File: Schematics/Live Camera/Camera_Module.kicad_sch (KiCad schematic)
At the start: 95 parts, among them J1 Stack Male Edge Connector, J2 SWD_01x04_Pin, J4 Therm_In, J4 USB_C_Female_USB2_Small, J5 VTX, J6 RunCam6, J7 VTX_BATT_IN, J8 VTX_BATT_SWITCH, Q3 AO3400A, Q3 AO3401A, Q4 AO3400A, Q5 AO3401A, Q6 AO3401A, SW1 SW_STM_RESET, SW2 SW_STM_BOOT_MODE, U1 CP2102N-Axx-xQFN28, U1 LM66100DCKR, U1 STM32F103CBT6, U12 AMS1117-3.3, U3 W25Q128JVS, U5 LM66100DCKR, U6 LM66100DCKR, U8 ISO1042BDWVR, Y1 X322516MMB4SI

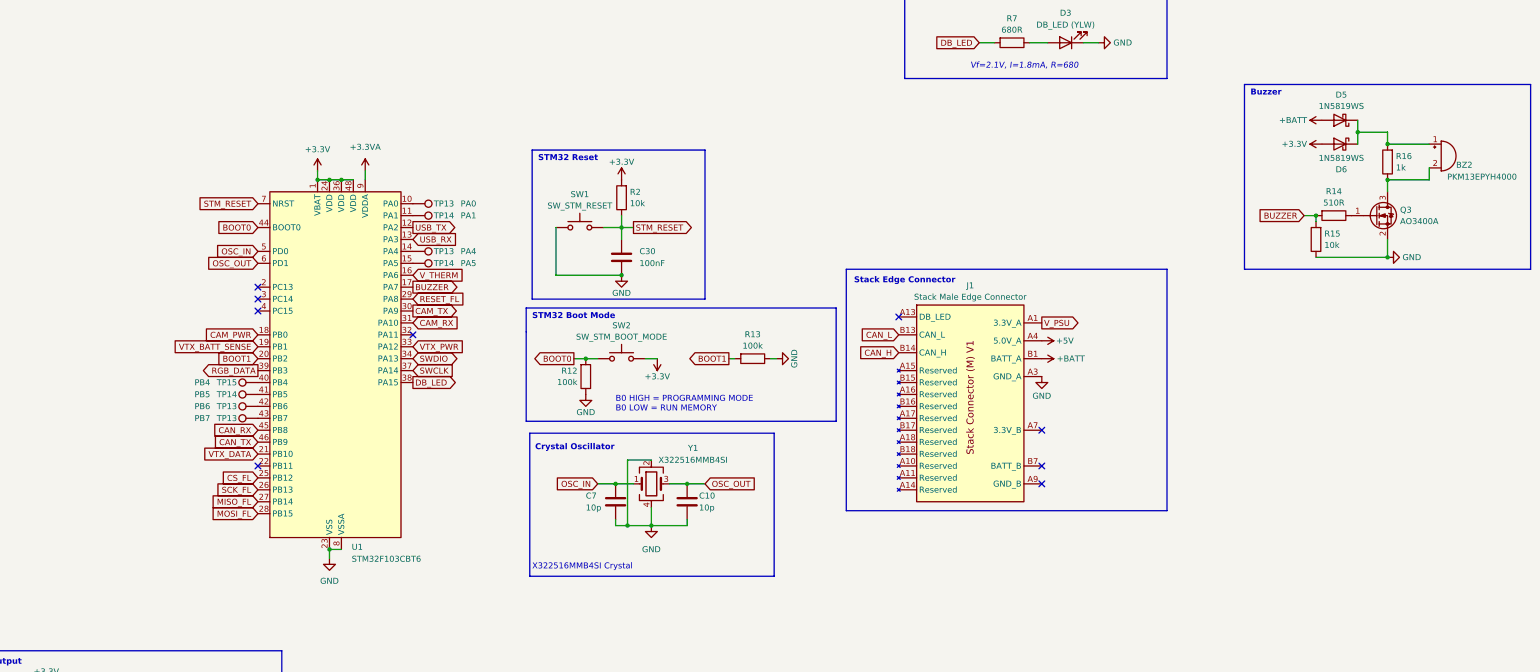
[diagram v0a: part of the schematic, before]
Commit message: Added revised buzzer circuit
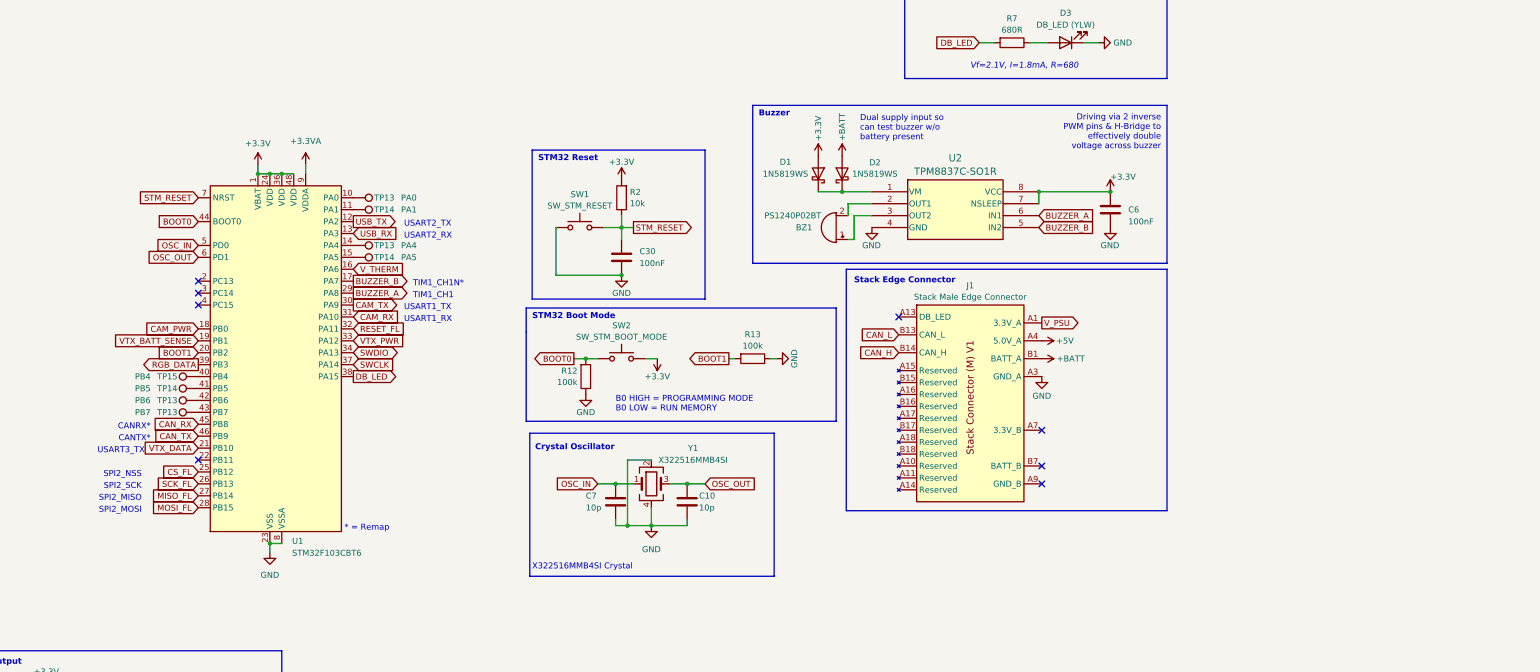
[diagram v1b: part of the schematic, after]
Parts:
- removed BZ2: PKM13EPYH4000, footprints:Buzzer_12.6x9.5RM5.0, symbol Device:Buzzer
- removed D5, D6: 1N5819WS, Diode_SMD:D_SOD-323, symbol Diode:1N5819WS
- removed Q3: AO3400A, Package_TO_SOT_SMD:SOT-23, symbol Transistor_FET:AO3400A
- removed R14: 510R, Resistor_SMD:R_0603_1608Metric, symbol Device:R
- removed R15: 10k, Resistor_SMD:R_0603_1608Metric, symbol Device:R
- removed R16: 1k, Resistor_SMD:R_0603_1608Metric, symbol Device:R
- added BZ1: PS1240P02BT, footprints:Buzzer_12.6x9.5RM5.0, symbol Device:Buzzer
- added C6: 100nF, Capacitor_SMD:C_0603_1608Metric, symbol Device:C
- added D1, D2: 1N5819WS, Diode_SMD:D_SOD-323, symbol Diode:1N5819WS
- added U2: TPM8837C-SO1R, footprints:SOP-8_TPK, symbol TPM8837C-SO1R:TPM8837C-SO1R
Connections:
- net +3.3V: now also C6.1, D1.2 (A), U2.7 (NSLEEP), U2.8 (VCC)
- net +BATT: now also D2.2 (A)
- net GND: now also C6.2, U2.4 (GND)
- net RESET_FL: now also U1.32 (PA11); no longer U1.29 (PA8)
- net BUZZER renamed BUZZER_B
- net BUZZER_B: now also U2.5 (IN2)
- new net: BZ1.1 (-), U2.3 (OUT2)
- new net: BZ1.2 (+), U2.2 (OUT1)
- new net: D1.1 (K), D2.1 (K), U2.1 (VM)
- new net BUZZER_A: U1.29 (PA8), U2.6 (IN1)
- no-connect marks 31 -> 30
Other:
- note added: "* = Remap"
- note added: "CANRX*"
- note added: "CANTX*"
- note added: "Driving via 2 inverse PWM pins & H-Bridge to effectively double voltage across buzzer"
- note added: "Dual supply input so can test buzzer w/o battery present"
- note added: "SPI2_MISO"
- note added: "SPI2_MOSI"
- note added: "SPI2_NSS"
- note added: "SPI2_SCK"
- note added: "TIM1_CH1"
- note added: "TIM1_CH1N*"
- note added: "USART1_RX"
- note added: "USART1_TX"
- note added: "USART2_RX"
- note added: "USART2_TX"
- note added: "USART3_TX"
- moved on the sheet: TP13, TP14, TP15, U1

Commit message: Tweaked part fields
Changed "LCSC" fields to "JLCPCB", and added missing JLCPCB/Digikey part numbers.

There may be some minor mismatches hiding somewhere; should do a manual review.
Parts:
- C10, C7: JLCPCB (none) -> C1634; LCSC C1634 -> (none)
- C11, C3, C31, C32: JLCPCB (none) -> C96446; LCSC C96446 -> (none)
- C12, C13, C15, C17: JLCPCB (none) -> C1525; LCSC C1525 -> (none)
- C19: JLCPCB (none) -> C57112; LCSC C57112 -> (none)
- C2, C3, C4, C6: JLCPCB (none) -> C15849; LCSC C15849 -> (none)
- C20, C21: JLCPCB (none) -> C28323; LCSC C28323 -> (none)
- C22, C23, C30, C8: JLCPCB (none) -> C14663; LCSC C14663 -> (none)
- D1: JLCPCB (none) -> C2297; LCSC C2297 -> (none)
- D3: JLCPCB (none) -> C72038; LCSC C72038 -> (none)
- FB1: JLCPCB (none) -> C1015; LCSC C1015 -> (none)
- J2: Digikey (none) -> 952-3233-ND
- J4: JLCPCB (none) -> C2936184; LCSC C2936184 -> (none)
- J4: Digikey (none) -> ED10561-ND
- J6: Digikey (none) -> ED10563-ND
- Q3, Q5, Q6: JLCPCB (none) -> C15127; LCSC C15127 -> (none)
- Q4: JLCPCB (none) -> C20917; LCSC C20917 -> (none)
- R10, R12, R13, R14, R38: JLCPCB (none) -> C25803; LCSC C25803 -> (none)
- R11, R39: JLCPCB (none) -> C23193; LCSC C23193 -> (none)
- R15: JLCPCB (none) -> C4184
- R2, R4, R6: JLCPCB (none) -> C25804; LCSC C25804 -> (none)
- R28, R29: JLCPCB (none) -> C23186; LCSC C23186 -> (none)
- R29: JLCPCB (none) -> C21190; LCSC C21190 -> (none)
- R30: JLCPCB (none) -> C31850; LCSC C31850 -> (none)
- R31: JLCPCB (none) -> C25819; LCSC C25819 -> (none)
- R5: JLCPCB (none) -> C22978; LCSC C22978 -> (none)
- R6: JLCPCB (none) -> C25804
- R7: JLCPCB (none) -> C23228; LCSC C23228 -> (none)
- R8: JLCPCB (none) -> C22843; LCSC C22843 -> (none)
- SW1, SW2: JLCPCB (none) -> C318884; LCSC C318884 -> (none)
- U1, U5, U6: JLCPCB (none) -> C2869734; LCSC C2869734 -> (none)
- U1: JLCPCB (none) -> C6568; LCSC C6568 -> (none)
- U1: JLCPCB (none) -> C8304; LCSC C8304 -> (none)
- U12: JLCPCB (none) -> C6186; LCSC C6186 -> (none)
- U3: JLCPCB (none) -> C97521; LCSC C97521 -> (none)
- U8: JLCPCB (none) -> C484409; LCSC C484409 -> (none)
- Y1: JLCPCB (none) -> C13738; LCSC C13738 -> (none)

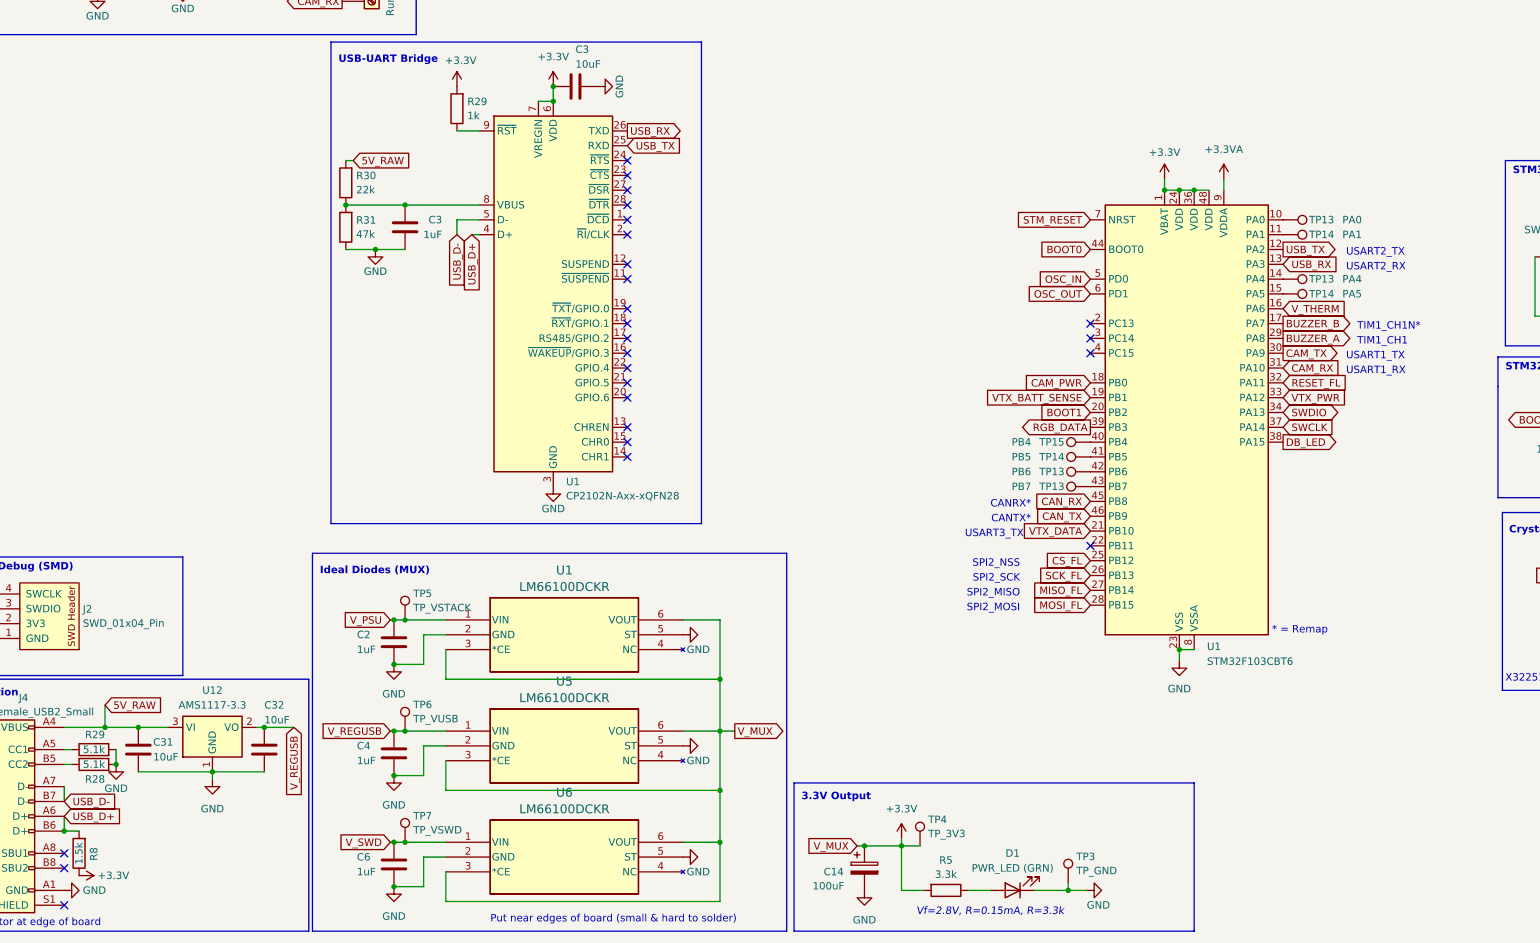
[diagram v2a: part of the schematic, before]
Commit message: Tweaks + 3D model additions
Added/tweaked some notes in the schematic, adjusted silkscreen on PCB + added "PB-FREE" label, updated SWD footprint, and added all missing 3D models to project.
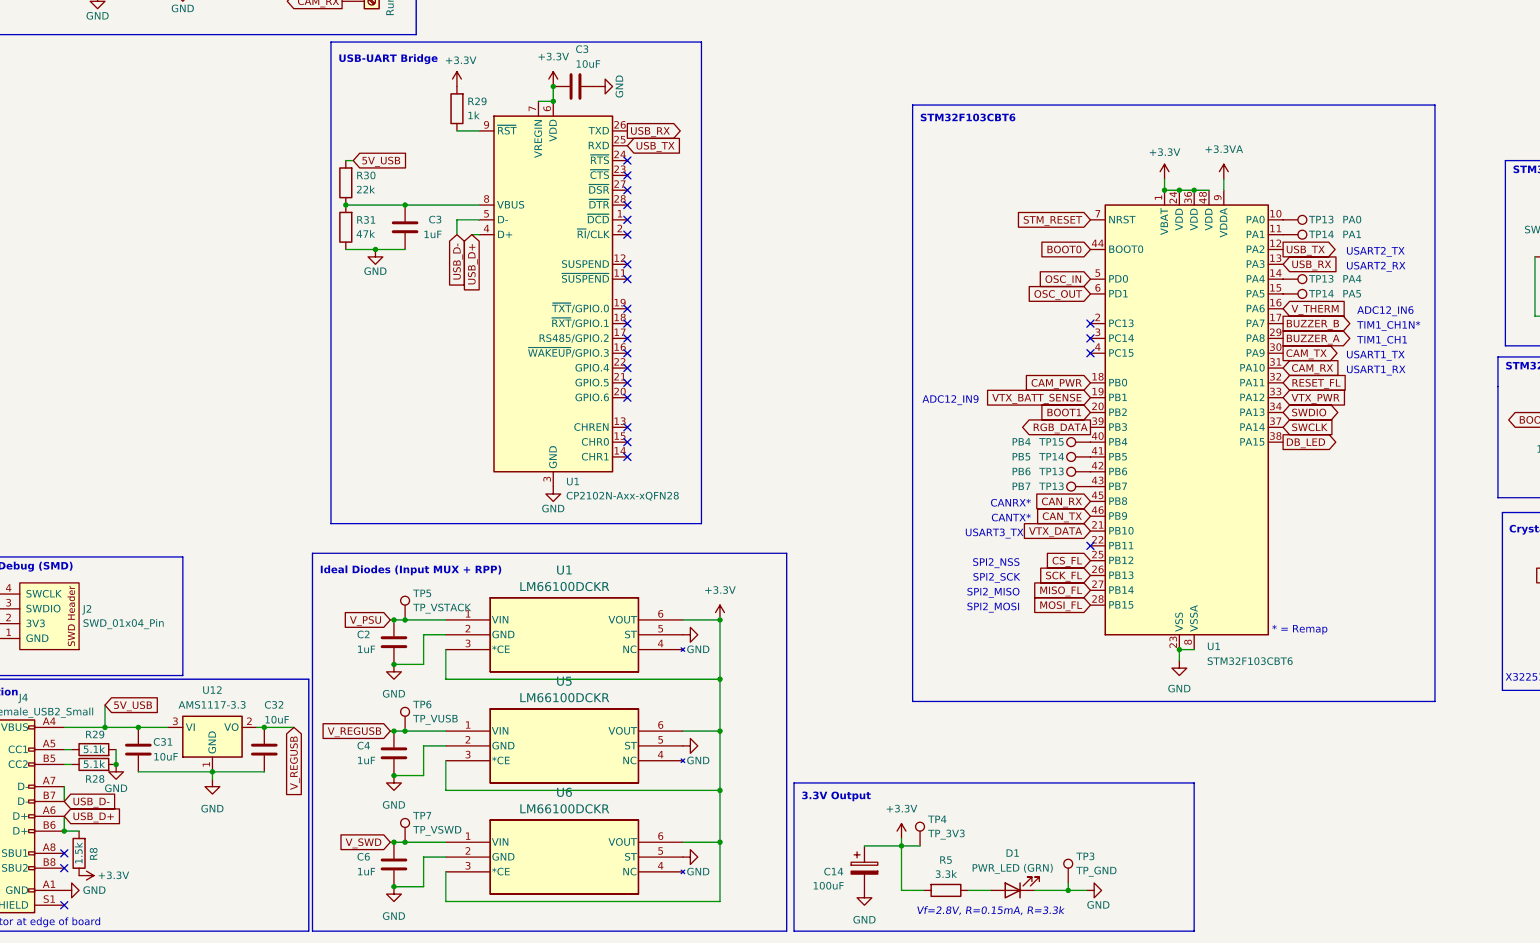
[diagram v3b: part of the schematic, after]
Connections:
- net 5V_RAW renamed 5V_USB
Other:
- note added: "ADC12_IN6"
- note added: "ADC12_IN9"
- note added: "Ideal Diodes (Input MUX + RPP)"
- note added: "STM32F103CBT6"
- note removed: "Ideal Diodes (MUX)"
- note removed: "Put near edges of board (small & hard to solder)"
- title: QRET 24-25 SRAD Camera Module (????) -> QRET 24-25 SRAD Camera Module (FizzBuzz? Ocellus?)
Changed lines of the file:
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@@
 	(paper "B")
 	(title_block
-		(title "QRET 24-25 SRAD Camera Module (????)")
-		(date "2025-02-20")
+		(title "QRET 24-25 SRAD Camera Module (FizzBuzz? Ocellus?)")
+		(date "2025-02-26")
 		(rev "V1.0")
 		(company "Queen's Rocket Engineering Team")
@@
 	)
 	(junction
+		(at 149.225 213.36)
+		(diameter 0)
+		(color 0 0 0 0)
+	)
+	(junction
 		(at 407.035 143.51)
 		(diameter 0)
@@
 	)
 	(junction
-		(at 173.99 252.095)
-		(diameter 0)
-		(color 0 0 0 0)
-	)
-	(junction
 		(at 172.72 40.005)
 		(diameter 0)
@@
 	(wire
 		(pts
-			(xy 172.72 252.095) (xy 173.99 252.095)
-		)
-		(stroke
-			(width 0)
-			(type default)
-		)
-	)
-	(wire
-		(pts
 			(xy 351.155 146.05) (xy 356.235 146.05)
 		)
@@
 	(wire
 		(pts
-			(xy 149.225 232.41) (xy 151.765 232.41)
-		)
-		(stroke
-			(width 0)
-			(type default)
-		)
-	)
-	(wire
-		(pts
 			(xy 25.4 48.895) (xy 44.45 48.895)
 		)
@@
 	)
 	(rectangle
+		(start 182.245 125.095)
+		(end 271.78 227.33)
+		(stroke
+			(width 0)
+			(type default)
+		)
+		(fill
+			(type none)
+		)
+	)
+	(rectangle
 		(start 339.725 59.69)
 		(end 361.95 97.155)
@@
 		)
 	)
-	(text "Put near edges of board (small & hard to solder)"
-		(exclude_from_sim no)
-		(at 109.855 265.43 0)
-		(effects
-			(font
-				(size 1.27 1.27)
-			)
-			(justify left bottom)
-		)
-	)
 	(text "Additional Filtering for Analogue VDD"
 		(exclude_from_sim no)
@@
 		)
 	)
+	(text "ADC12_IN9"
+		(exclude_from_sim no)
+		(at 193.675 176.53 0)
+		(effects
+			(font
+				(size 1.27 1.27)
+			)
+			(justify right bottom)
+		)
+	)
 	(text "Crystal Oscillator"
 		(exclude_from_sim no)
@@
 		)
 	)
+	(text "STM32F103CBT6"
+		(exclude_from_sim no)
+		(at 183.515 128.27 0)
+		(effects
+			(font
+				(size 1.27 1.27)
+				(thickness 0.254)
+				(bold yes)
+			)
+			(justify left bottom)
+		)
+	)
+	(text "ADC12_IN6"
+		(exclude_from_sim no)
+		(at 258.445 161.29 0)
+		(effects
+			(font
+				(size 1.27 1.27)
+			)
+			(justify left bottom)
+		)
+	)
 	(text "Serial Wire Debug (SMD)"
 		(exclude_from_sim no)
@@
 		)
 	)
-	(text "Ideal Diodes (MUX)"
+	(text "Ideal Diodes (Input MUX + RPP)"
 		(exclude_from_sim no)
 		(at 80.645 205.74 0)
@@
 		)
 	)
-	(global_label "5V_RAW"
+	(global_label "5V_USB"
 		(shape input)
 		(at 43.815 227.965 0)
@@
 		)
 	)
-	(global_label "V_MUX"
-		(shape input)
-		(at 172.72 252.095 180)
-		(fields_autoplaced yes)
-		(effects
-			(font
-				(size 1.27 1.27)
-			)
-			(justify right)
-		)
-		(property "Intersheetrefs" "${INTERSHEET_REFS}"
-			(at 163.6872 252.095 0)
-			(effects
-				(font
-					(size 1.27 1.27)
-				)
-				(justify right)
-				(hide yes)
-			)
-		)
-	)
 	(global_label "V_SWD"
 		(shape output)
@@
 		)
 	)
-	(global_label "5V_RAW"
+	(global_label "5V_USB"
 		(shape input)
 		(at 86.36 134.62 0)
@@
 		)
 	)
-	(global_label "V_MUX"
-		(shape output)
-		(at 151.765 232.41 0)
-		(fields_autoplaced yes)
-		(effects
-			(font
-				(size 1.27 1.27)
-			)
-			(justify left)
-		)
-		(property "Intersheetrefs" "${INTERSHEET_REFS}"
-			(at 160.7978 232.41 0)
-			(effects
-				(font
-					(size 1.27 1.27)
-				)
-				(justify left)
-				(hide yes)
-			)
-		)
-	)
 	(global_label "CAN_L"
 		(shape input)
@@
 					(unit 1)
 				)
+			)
+		)
+	)
+	(symbol
+		(lib_id "power:+3.3V")
+		(at 149.225 213.36 0)
+		(unit 1)
+		(exclude_from_sim no)
+		(in_bom yes)
+		(on_board yes)
+		(dnp no)
+		(fields_autoplaced yes)
+		(property "Reference" "#PWR06"
+			(at 149.225 217.17 0)
+			(effects
+				(font
+					(size 1.27 1.27)
+				)
+				(hide yes)
+			)
+		)
+		(property "Value" "+3.3V"
+			(at 149.225 208.28 0)
+			(effects
+				(font
+					(size 1.27 1.27)
+				)
+			)
+		)
+		(property "Footprint" ""
+			(at 149.225 213.36 0)
+			(effects
+				(font
+					(size 1.27 1.27)
+				)
+				(hide yes)
+			)
+		)
+		(property "Datasheet" ""
+			(at 149.225 213.36 0)
+			(effects
+				(font
+					(size 1.27 1.27)
+				)
+				(hide yes)
+			)
+		)
+		(property "Description" ""
+			(at 149.225 213.36 0)
+			(effects
+				(font
+					(size 1.27 1.27)
+				)
+				(hide yes)
+			)
+		)
+		(pin "1"
+		)
+		(instances
+			(project "Camera_Module"
+				(path "/e77d0584-110f-4b35-98c2-0ebac97a828e"
+					(reference "#PWR06")
+					(unit 1)
+				)
